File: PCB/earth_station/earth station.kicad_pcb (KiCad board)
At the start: 2 copper layers, 50 x 50 mm, 10 parts, among them P1 CONN_01X02, U1 ARDUPROMINI, U2 RFM95, U3 LM2596_DC-DC

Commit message: Move Logos
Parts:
- moved REF** 2.80 mm to (147.3, 91.4)
- moved G*** 1.19 mm to (144.8, 94.0)
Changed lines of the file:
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@@
-(kicad_pcb (version 4) (host pcbnew 4.0.0-rc1-stable)
+(kicad_pcb (version 4) (host pcbnew 4.0.3-stable)
   (general
     (links 24)
-    (no_connects 18)
+    (no_connects 0)
     (area 109.049999 72.599999 159.200001 122.750001)
     (thickness 1.6)
@@
   )
   (module Symbols:Symbol_OSHW-Logo_SilkScreen_BIG (layer B.Cu)
-    (at 149 89.2 180)
+    (at 147.32 91.44 180)
     (descr "Symbol, OSHW-Logo, Silk Screen, BIG")
     (tags "Symbol, OSHW-Logo, Silk Screen, BIG")
@@
   )
   (module theinventorhouse:electronic_cats_logo_8x6 (layer B.Cu)
-    (at 144.9 92.8 180)
+    (at 144.78 93.98 180)
     (fp_text reference G*** (at 0 0 180) (layer B.SilkS) hide
       (effects (font (thickness 0.3)) (justify mirror))
@@
   (gr_circle (center 156.475 119.85) (end 156.575 121.4) (layer Edge.Cuts) (width 0.15))
   (gr_circle (center 112.1 75.15) (end 112.2 76.7) (layer Edge.Cuts) (width 0.15))
-  (gr_text "CatSat I" (at 127.1 93) (layer B.SilkS)
+  (gr_text "CatSat I" (at 144.78 88.9) (layer B.SilkS)
     (effects (font (size 1.5 1.5) (thickness 0.3)) (justify mirror))
   )

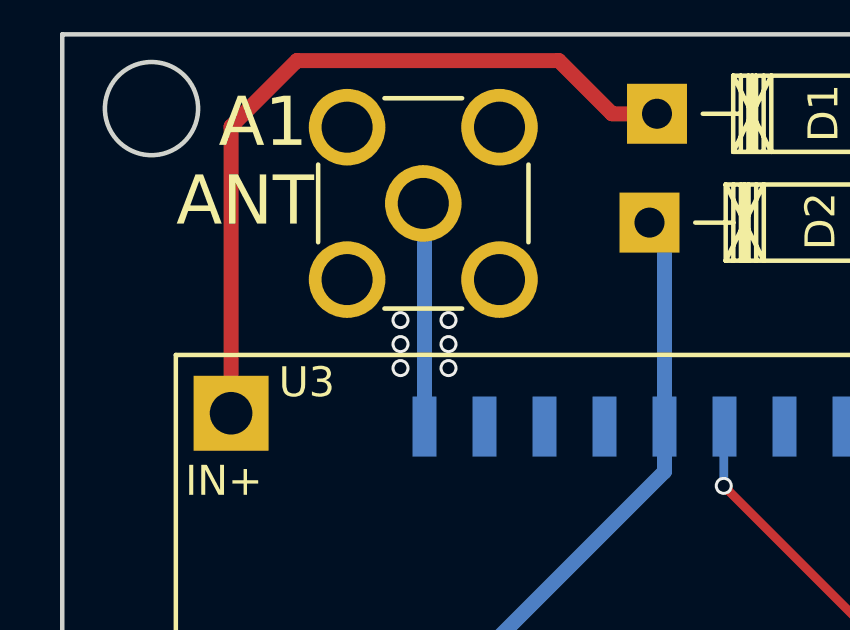
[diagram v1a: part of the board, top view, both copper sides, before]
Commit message: Via fix again
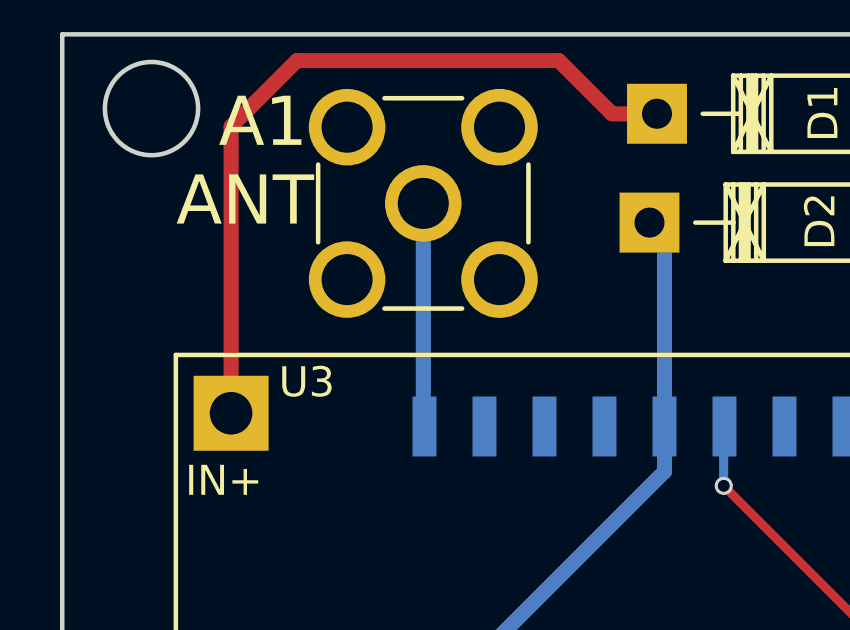
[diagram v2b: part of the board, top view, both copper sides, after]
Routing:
- net GND: track 1.89 -> 2.80 mm
- net (no net): vias 6 -> 0
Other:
- net class ANT added: clearance 0.1, trace_width 0.5, via_dia 0.6, via_drill 0.4
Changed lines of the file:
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@@
-(kicad_pcb (version 4) (host pcbnew 4.0.3-stable)
+(kicad_pcb (version 4) (host pcbnew 4.0.0-rc1-stable)
   (general
     (links 24)
     (no_connects 0)
-    (area 109.049999 72.599999 159.200001 122.750001)
+    (area 109.049999 72.02246 159.200001 122.750001)
     (thickness 1.6)
     (drawings 10)
-    (tracks 67)
+    (tracks 64)
     (zones 0)
     (modules 10)
@@
     (add_net "Net-(U2-Pad9)")
   )
+  (net_class ANT ""
+    (clearance 0.1)
+    (trace_width 0.5)
+    (via_dia 0.6)
+    (via_drill 0.4)
+    (uvia_dia 0.3)
+    (uvia_drill 0.1)
+    (add_net "Net-(A1-Pad1)")
+  )
   (net_class Vcc ""
     (clearance 0.4)
@@
     (uvia_drill 0.1)
     (add_net "(+3.3)")
-    (add_net "Net-(A1-Pad1)")
     (add_net "Net-(D1-Pad1)")
     (add_net "Net-(D1-Pad2)")
@@
   (gr_line (start 159.125 72.675) (end 159.125 122.675) (layer Edge.Cuts) (width 0.15))
   (gr_line (start 109.125 72.675) (end 159.125 72.675) (layer Edge.Cuts) (width 0.15))
-  (via (at 122 82.2) (size 0.6) (drill 0.4) (layers F.Cu B.Cu) (net 0))
-  (via (at 120.4 82.2) (size 0.6) (drill 0.4) (layers F.Cu B.Cu) (net 0))
-  (via (at 120.4 83.8) (size 0.6) (drill 0.4) (layers F.Cu B.Cu) (net 0))
-  (via (at 122 83.8) (size 0.6) (drill 0.4) (layers F.Cu B.Cu) (net 0))
-  (via (at 120.4 83) (size 0.6) (drill 0.4) (layers F.Cu B.Cu) (net 0))
-  (via (at 122 83) (size 0.6) (drill 0.4) (layers F.Cu B.Cu) (net 0))
-  (segment (start 121.2 85.75) (end 121.2 78.35) (width 0.5) (layer B.Cu) (net 1))
+  (segment (start 121.16 78.31) (end 121.16 85.71) (width 0.5) (layer B.Cu) (net 1))
+  (segment (start 121.16 85.71) (end 121.2 85.75) (width 0.5) (layer B.Cu) (net 1))
   (segment (start 121.2 78.35) (end 121.16 78.31) (width 0.5) (layer B.Cu) (net 1))
+  (segment (start 118.62 80.85) (end 118.89999 80.85) (width 0.3) (layer F.Cu) (net 2))
+  (segment (start 118.62 80.85) (end 119.25 80.85) (width 0.3) (layer F.Cu) (net 2))
   (segment (start 135.2 101.95) (end 135.2 100.1) (width 0.3) (layer B.Cu) (net 2))
   (segment (start 135.2 100.1) (end 135.175 100.075) (width 0.3) (layer B.Cu) (net 2))
